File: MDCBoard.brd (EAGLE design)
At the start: 43.9 x 32.6 mm, 201 parts, among them J1 JUMPER-SOLDER, J10 MICROSD-SOCKET, J11 USB-C-RECEPTACLE-KOREANHRO, J2 JUMPER-SOLDER, J3 JUMPER-SOLDER, J4 JUMPER-SOLDER, J5 JST-SM02B-SRSS-TB, J6 JUMPER-SOLDER, J7 JUMPER-SOLDER, J8 JUMPER-SOLDER, Q1 PMOS-NEXPERIA-SOT1220, Q2 PMOS-NEXPERIA-SOT1220, Q3 PMOS-NEXPERIA-SOT1220, Q4 DIODESINC-DMG2305UX, Q5 DIODESINC-DMG2305UX, Q6 DIODESINC-DMG2305UX, Q7 DIODESINC-DMG2305UX, Q8 DIODESINC-DMG2305UX, SW1 TACTILE-SWITCH, U1 TI-TPS2116, U10 TI-TPS22919DCK, U11 TI-TPS22919DCK, U12 TI-TPS22919DCK, U13 TI-TPS22919DCK, U15 TI-MSP430FR2433IRGE, U16 TI-TXB0102, U17 PANASONIC-EKMB110711X, U18 LATTICE-ICE40HX4K-BG121, U19 WINBOND-W25Q40EW, U2 DIODESINC-AP7350, U20 NEXPERIA-74LVC1G98-OR-INV-INP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, U21 NEXPERIA-74LVC1G98-BUFFER, U22 ON-AR0330CS1C12SPKA0, U23 ALLIANCE-AS4C8M16MSA-6BIN, U24 STM-STM32F730, U25 DIODESINC-DT1446-04V-7, U26 NEXPERIA-74LVC1G98-INVERTER, U3 NEXPERIA-74LVC1G98-NOR, U4 MICROCHIP-MCP7383X, U5 NEXPERIA-74LVC1G98-INVERTER, U6 EATON-STN101, U7 TI-TPS62A01, U8 TI-TPS62A01, U9 TI-TPS62A01, X1 EPSON-FC-135, X2 SITIME-SIT8021, X3 SITIME-SIT8021

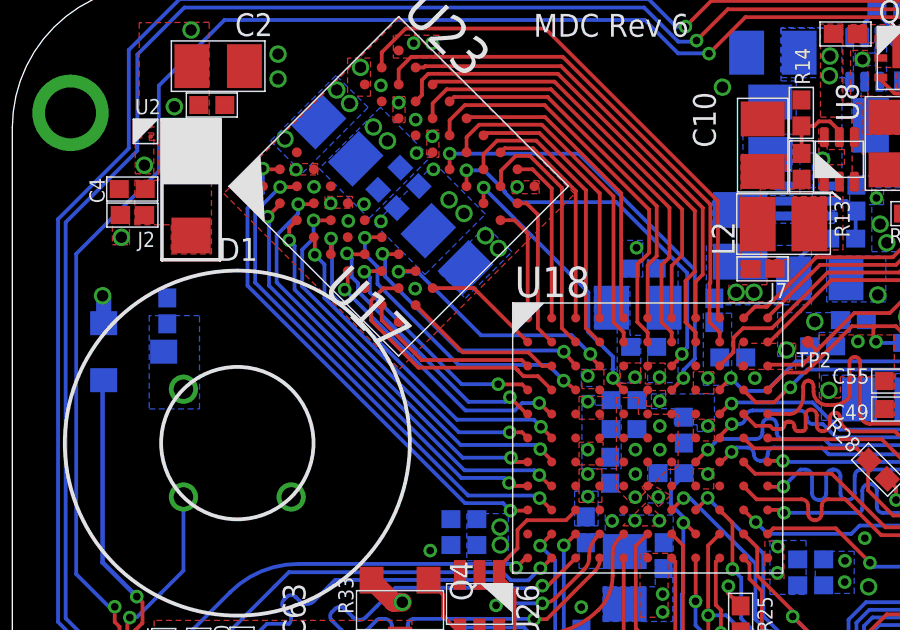
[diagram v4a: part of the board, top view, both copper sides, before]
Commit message: Adjust RAM routing
* RAMClkTraceLen                            = 12.264 mm
* ShortestRAMTraceLen                       =  7.387 mm (-4.877 mm)
* LongestRAMTraceLen                        = 18.407 mm (+6.143 mm)

* Vp [speed of signals in F4-4]             = 0.1524 mm / ps
* f [RAM frequency]                         = 108 MHz
* TClkPeriod                                = 9.26 ns

* Timing differences between shortest/longest trace and clock trace

    - TDiffShortest                             = (ShortestRAMTraceLen-RAMClkTraceLen) / Vp
                                                = -32 ps

    - TDiffLongest                              = (LongestRAMTraceLen-RAMClkTraceLen) / Vp
                                                = 40 ps

* Timing differences as fraction of clock period

    - TDiffFracShortest                         = TDiffShortest / TClkPeriod
                                                = -0.346%

    - TDiffFracLongest                          = TDiffLongest / TClkPeriod
                                                = 0.432%
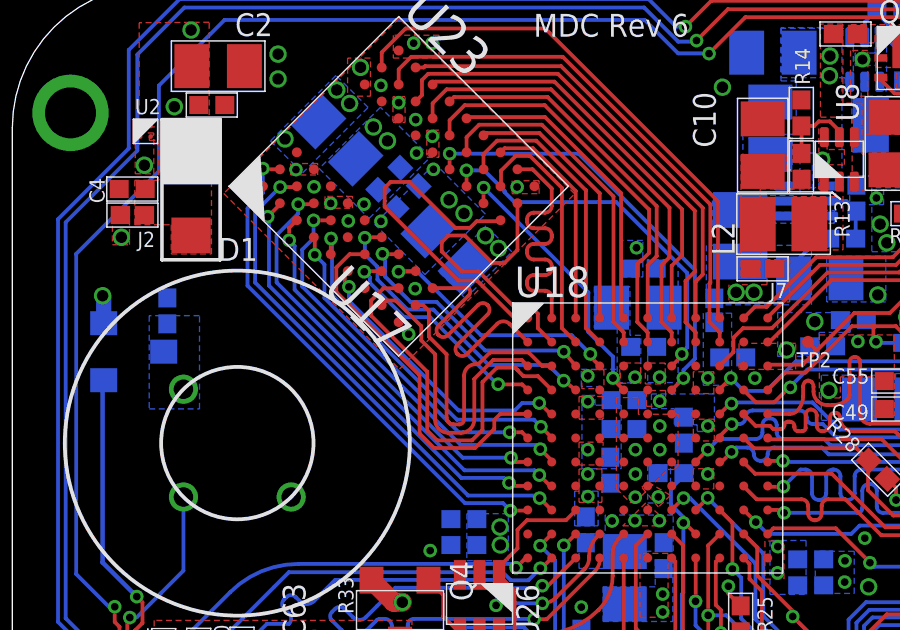
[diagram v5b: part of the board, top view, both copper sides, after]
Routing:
- net RAM_A3: track 3.95 -> 11.6 mm
- net RAM_A4: track 3.91 -> 10.3 mm
- net RAM_A2: track 5.27 -> 10.3 mm
- net RAM_A5: track 5.38 -> 9.96 mm
- net RAM_A8: track 6.00 -> 10.2 mm
- net RAM_A7: track 8.74 -> 12.7 mm
- net RAM_A10: track 5.72 -> 9.09 mm
- net RAM_CLK: track 9.51 -> 12.3 mm, vias 2 -> 0
- net GND: vias 79 -> 80

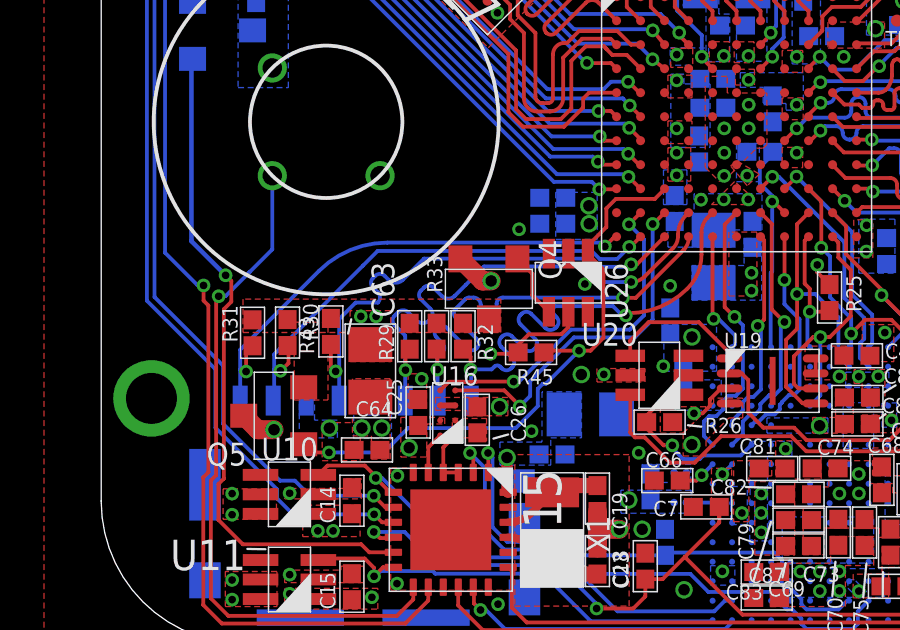
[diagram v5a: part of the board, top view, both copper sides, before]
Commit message: Length-match SD traces
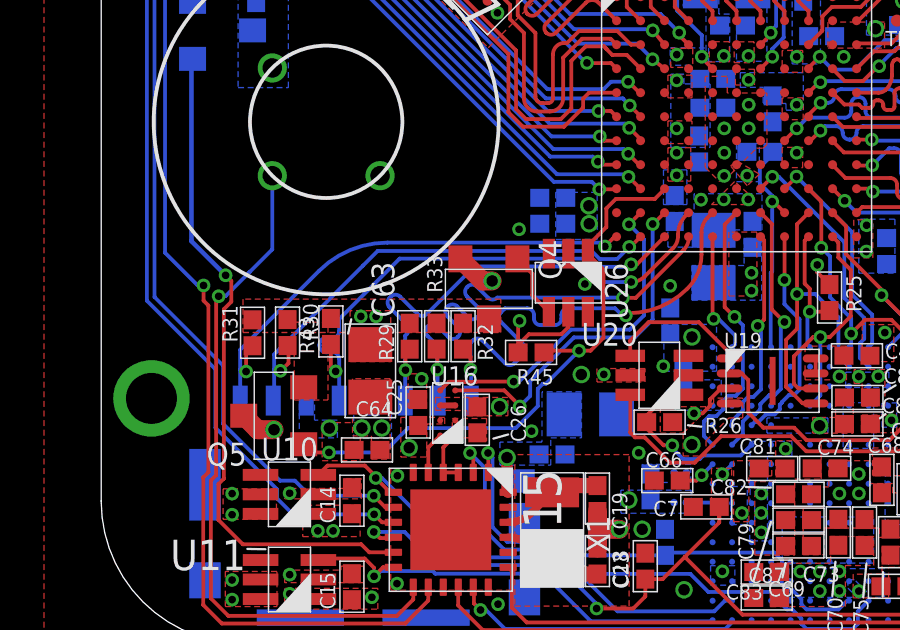
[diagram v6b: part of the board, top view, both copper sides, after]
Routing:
- net VDD_B_2V8_IMG_SD: track 75.7 -> 77.0 mm

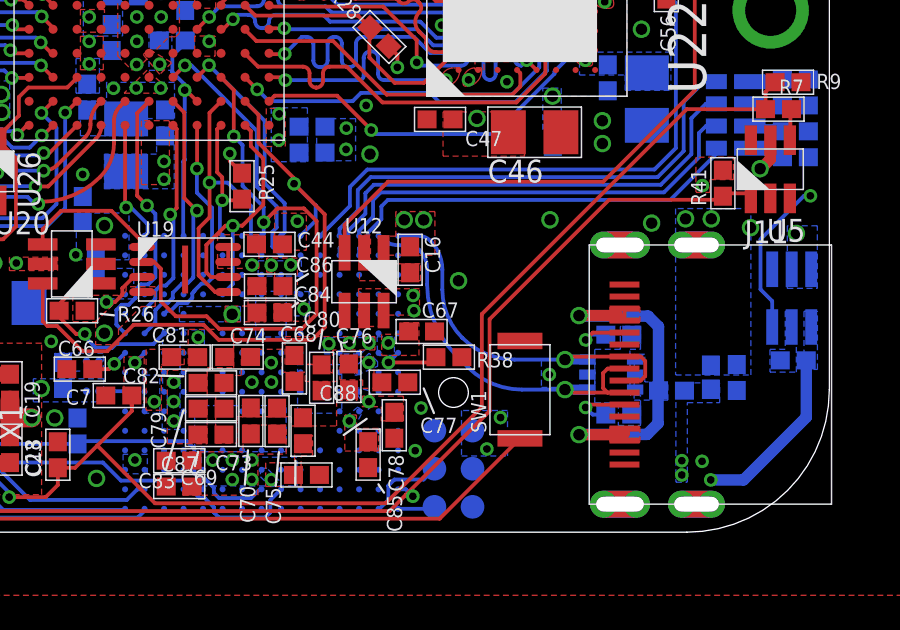
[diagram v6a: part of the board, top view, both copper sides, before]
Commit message: Add keepout region for button stopper making contact with button
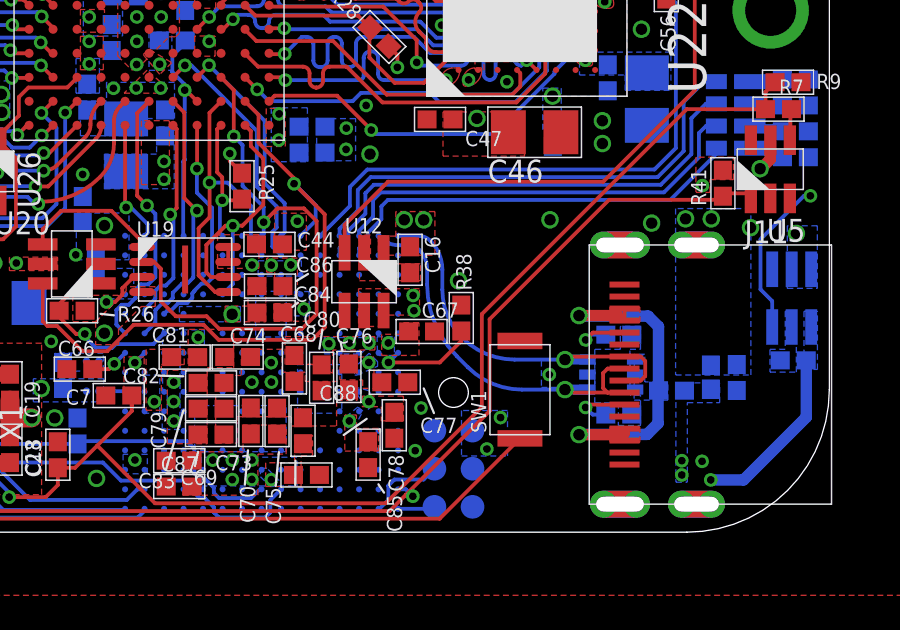
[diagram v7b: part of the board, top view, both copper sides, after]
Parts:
- moved R38 1.37 mm to (31.6, 7.14), turned to 270 degrees
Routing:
- net N$10: track 2.11 -> 3.51 mm
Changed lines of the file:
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@@
 <text x="38.3667" y="23.1013" size="0.508" layer="26" font="vector" rot="MR0">LED1-4</text>
 <circle x="33.5424" y="17.392" radius="6.63935" width="1.75" layer="39"/>
+<circle x="33.5424" y="4.75" radius="1.8" width="0" layer="39"/>
 </plain>
 <attributes>
@@
 <attribute name="PN" value="TMK105CBJ225KV-F" x="30.263415625" y="6.69100625" size="1.778" layer="27" display="off"/>
 </element>
-<element name="R38" library="EagleLibrary" package="0402" value="3k" x="31.174215625" y="5.833159375" smashed="yes" rot="R180">
-<attribute name="MFG" value="Yageo" x="31.174215625" y="5.833159375" size="1.778" layer="27" rot="R180" display="off"/>
-<attribute name="NAME" x="33.327753125" y="6.001059375" size="0.508" layer="25" font="vector" rot="R180"/>
-<attribute name="PN" value="AC0402FR-073KL" x="31.174215625" y="5.833159375" size="1.778" layer="27" rot="R180" display="off"/>
+<element name="R38" library="EagleLibrary" package="0402" value="3k" x="31.587215625" y="7.138159375" smashed="yes" rot="R270">
+<attribute name="MFG" value="Yageo" x="31.587215625" y="7.138159375" size="1.778" layer="27" rot="R270" display="off"/>
+<attribute name="NAME" x="31.419315625" y="9.291696875" size="0.508" layer="25" font="vector" rot="R270"/>
+<attribute name="PN" value="AC0402FR-073KL" x="31.587215625" y="7.138159375" size="1.778" layer="27" rot="R270" display="off"/>
 </element>
 <element name="C66" library="EagleLibrary" package="0402" value="100n" x="18.870203125" y="5.433821875" smashed="yes" rot="R180">
@@
 <wire x1="29.158371875" y1="5.6569875" x2="29.157765625" y2="5.6569875" width="0.127" layer="16"/>
 <via x="29.157765625" y="5.6569875" extent="1-16" drill="0.254"/>
-<wire x1="30.741715625" y1="5.833159375" x2="30.56554375" y2="5.6569875" width="0.127" layer="1"/>
-<wire x1="30.56554375" y1="5.6569875" x2="29.157765625" y2="5.6569875" width="0.127" layer="1"/>
+<wire x1="31.587215625" y1="6.705659375" x2="31.587215625" y2="6.372921875" width="0.127" layer="1"/>
+<wire x1="31.587215625" y1="6.372921875" x2="30.87128125" y2="5.6569875" width="0.127" layer="1"/>
+<wire x1="30.87128125" y1="5.6569875" x2="29.157765625" y2="5.6569875" width="0.127" layer="1"/>
 </signal>
 <signal name="N$25">

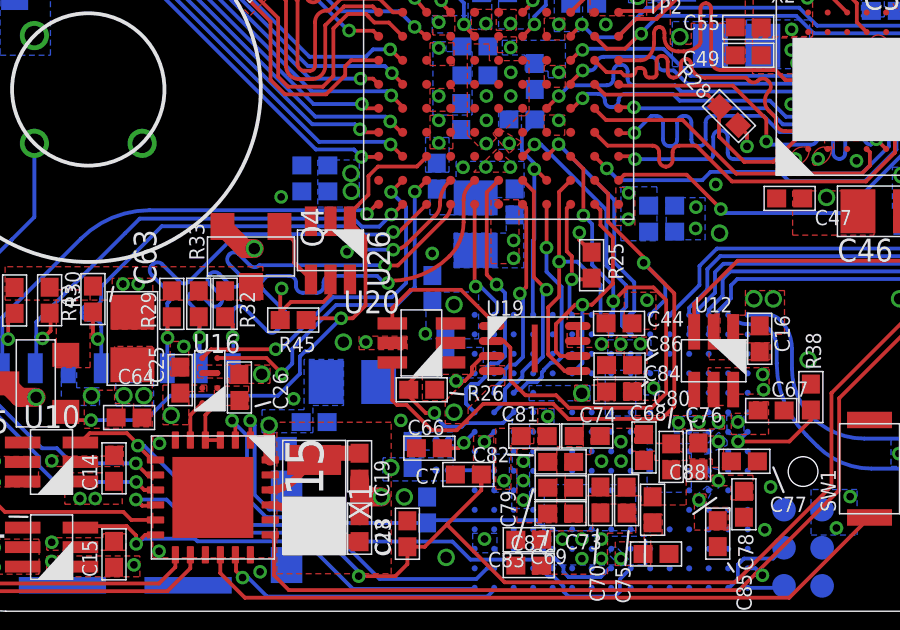
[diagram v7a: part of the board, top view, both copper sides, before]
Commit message: Fix VDDA/VREF+ voltages -- apparently they need to be the same voltage as VDD (1.8V), but we increased them to 3.3V. Yikes.
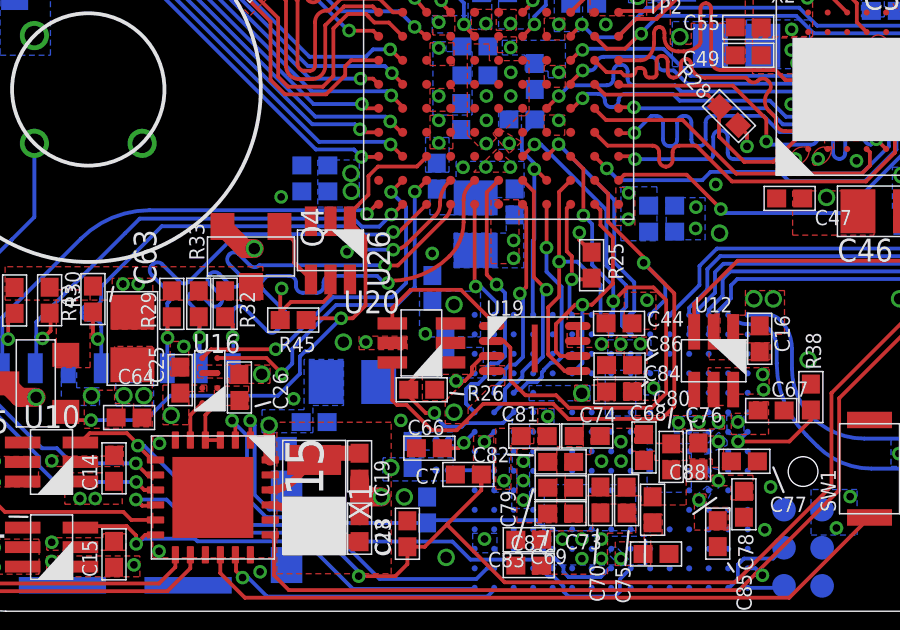
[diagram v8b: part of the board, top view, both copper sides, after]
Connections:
- net VDD_B_1V8_STM: now also C71.1, C72.1, U24.P1, U24.R1
- net VDD_B_3V3_STM: no longer C71.1, C72.1, U24.P1, U24.R1
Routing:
- net VDD_B_3V3_STM: track 36.5 -> 22.5 mm, vias 4 -> 3
- net VDD_B_1V8_STM: track 59.3 -> 64.4 mm, vias 20 -> 21
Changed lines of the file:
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@@
 <grid distance="10" unitdist="mil" unit="mil" style="lines" multiple="1" display="no" altdistance="0.00254" altunitdist="mm" altunit="mil"/>
 <layers>
-<layer number="1" name="Top" color="4" fill="1" visible="yes" active="yes"/>
+<layer number="1" name="Top" color="4" fill="1" visible="no" active="yes"/>
 <layer number="2" name="Ground" color="16" fill="1" visible="no" active="yes"/>
 <layer number="3" name="Route3" color="17" fill="1" visible="no" active="no"/>
@@
 <layer number="14" name="Route14" color="22" fill="1" visible="no" active="no"/>
 <layer number="15" name="Power" color="42" fill="1" visible="no" active="yes"/>
-<layer number="16" name="Bottom" color="1" fill="1" visible="no" active="yes"/>
+<layer number="16" name="Bottom" color="1" fill="1" visible="yes" active="yes"/>
 <layer number="17" name="Pads" color="2" fill="1" visible="yes" active="yes"/>
 <layer number="18" name="Vias" color="2" fill="1" visible="yes" active="yes"/>
 <layer number="19" name="Unrouted" color="6" fill="1" visible="no" active="yes"/>
 <layer number="20" name="Dimension" color="24" fill="1" visible="yes" active="yes"/>
-<layer number="21" name="tPlace" color="7" fill="1" visible="yes" active="yes"/>
-<layer number="22" name="bPlace" color="7" fill="1" visible="no" active="yes"/>
-<layer number="23" name="tOrigins" color="15" fill="1" visible="yes" active="yes"/>
-<layer number="24" name="bOrigins" color="15" fill="1" visible="no" active="yes"/>
-<layer number="25" name="tNames" color="7" fill="1" visible="yes" active="yes"/>
-<layer number="26" name="bNames" color="7" fill="1" visible="no" active="yes"/>
-<layer number="27" name="tValues" color="7" fill="1" visible="yes" active="yes"/>
-<layer number="28" name="bValues" color="7" fill="1" visible="no" active="yes"/>
-<layer number="29" name="tStop" color="7" fill="3" visible="yes" active="yes"/>
-<layer number="30" name="bStop" color="7" fill="6" visible="no" active="yes"/>
-<layer number="31" name="tCream" color="7" fill="4" visible="yes" active="yes"/>
-<layer number="32" name="bCream" color="7" fill="5" visible="no" active="yes"/>
-<layer number="33" name="tFinish" color="6" fill="3" visible="yes" active="yes"/>
-<layer number="34" name="bFinish" color="6" fill="6" visible="no" active="yes"/>
-<layer number="35" name="tGlue" color="7" fill="4" visible="yes" active="yes"/>
-<layer number="36" name="bGlue" color="7" fill="5" visible="no" active="yes"/>
-<layer number="37" name="tTest" color="7" fill="1" visible="yes" active="yes"/>
-<layer number="38" name="bTest" color="7" fill="1" visible="no" active="yes"/>
-<layer number="39" name="tKeepout" color="4" fill="11" visible="yes" active="yes"/>
-<layer number="40" name="bKeepout" color="1" fill="11" visible="no" active="yes"/>
-<layer number="41" name="tRestrict" color="4" fill="10" visible="yes" active="yes"/>
-<layer number="42" name="bRestrict" color="1" fill="10" visible="no" active="yes"/>
+<layer number="21" name="tPlace" color="7" fill="1" visible="no" active="yes"/>
+<layer number="22" name="bPlace" color="7" fill="1" visible="yes" active="yes"/>
+<layer number="23" name="tOrigins" color="15" fill="1" visible="no" active="yes"/>
+<layer number="24" name="bOrigins" color="15" fill="1" visible="yes" active="yes"/>
+<layer number="25" name="tNames" color="7" fill="1" visible="no" active="yes"/>
+<layer number="26" name="bNames" color="7" fill="1" visible="yes" active="yes"/>
+<layer number="27" name="tValues" color="7" fill="1" visible="no" active="yes"/>
+<layer number="28" name="bValues" color="7" fill="1" visible="yes" active="yes"/>
+<layer number="29" name="tStop" color="7" fill="3" visible="no" active="yes"/>
+<layer number="30" name="bStop" color="7" fill="6" visible="yes" active="yes"/>
+<layer number="31" name="tCream" color="7" fill="4" visible="no" active="yes"/>
+<layer number="32" name="bCream" color="7" fill="5" visible="yes" active="yes"/>
+<layer number="33" name="tFinish" color="6" fill="3" visible="no" active="yes"/>
+<layer number="34" name="bFinish" color="6" fill="6" visible="yes" active="yes"/>
+<layer number="35" name="tGlue" color="7" fill="4" visible="no" active="yes"/>
+<layer number="36" name="bGlue" color="7" fill="5" visible="yes" active="yes"/>
+<layer number="37" name="tTest" color="7" fill="1" visible="no" active="yes"/>
+<layer number="38" name="bTest" color="7" fill="1" visible="yes" active="yes"/>
+<layer number="39" name="tKeepout" color="4" fill="11" visible="no" active="yes"/>
+<layer number="40" name="bKeepout" color="1" fill="11" visible="yes" active="yes"/>
+<layer number="41" name="tRestrict" color="4" fill="10" visible="no" active="yes"/>
+<layer number="42" name="bRestrict" color="1" fill="10" visible="yes" active="yes"/>
 <layer number="43" name="vRestrict" color="2" fill="10" visible="no" active="yes"/>
 <layer number="44" name="Drills" color="7" fill="1" visible="no" active="yes"/>
@@
 <wire x1="42.498521875" y1="9.398" x2="42.878" y2="9.398" width="0.127" layer="15"/>
 <wire x1="42.878" y1="9.398" x2="43.23944375" y2="9.75944375" width="0.127" layer="15"/>
+<contactref element="U24" pad="P1"/>
+<contactref element="U24" pad="R1"/>
+<contactref element="C71" pad="1"/>
+<contactref element="C72" pad="1"/>
+<polygon width="0.127" layer="16" thermals="no">
+<vertex x="18.542" y="10.668"/>
+<vertex x="18.542" y="9.144"/>
+<vertex x="20.574" y="9.144"/>
+<vertex x="20.574" y="10.668"/>
+</polygon>
+<via x="19.692621875" y="10.220959375" extent="1-16" drill="0.381"/>
+<wire x1="22.817121875" y1="6.4923375" x2="22.817121875" y2="7.096459375" width="0.381" layer="15"/>
+<wire x1="22.817121875" y1="7.096459375" x2="19.692621875" y2="10.220959375" width="0.381" layer="15"/>
 </signal>
 <signal name="VDD_B_1V8_IMG_SD">
@@
 <wire x1="42.559796875" y1="9.959340625" x2="41.19185" y2="8.75598125" width="0.381" layer="15"/>
 <wire x1="41.19185" y1="8.75598125" x2="33.02906875" y2="8.75598125" width="0.381" layer="15"/>
-<contactref element="U24" pad="R1"/>
-<contactref element="U24" pad="H13"/>
-<contactref element="U24" pad="C8"/>
-<contactref element="U24" pad="P1"/>
-<contactref element="C71" pad="1"/>
-<contactref element="C72" pad="1"/>
-<via x="19.692621875" y="10.220959375" extent="1-16" drill="0.381"/>
-<polygon width="0.127" layer="16" thermals="no">
-<vertex x="18.756375" y="10.638584375"/>
-<vertex x="18.756375" y="9.079021875"/>
-<vertex x="20.51151875" y="9.079021875"/>
-<vertex x="20.51151875" y="10.638584375"/>
-</polygon>
-<wire x1="19.692621875" y1="10.220959375" x2="19.704721875" y2="10.220959375" width="0.381" layer="15"/>
-<wire x1="32.11420625" y1="9.67084375" x2="33.02906875" y2="8.75598125" width="0.381" layer="15"/>
-<wire x1="19.704721875" y1="10.220959375" x2="20.2548375" y2="9.67084375" width="0.381" layer="15"/>
-<wire x1="20.2548375" y1="9.67084375" x2="32.11420625" y2="9.67084375" width="0.381" layer="15"/>
 <via x="25.255521875" y="1.750159375" extent="1-16" drill="0.254"/>
 <polygon width="0.127" layer="16" thermals="no">
@@
 </polygon>
 <contactref element="C73" pad="1"/>
+<contactref element="U24" pad="H13"/>
+<contactref element="U24" pad="C8"/>
 </signal>
 <signal name="N$14">
